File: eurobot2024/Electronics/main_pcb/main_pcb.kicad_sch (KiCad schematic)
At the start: 58 parts, among them J1 PI40HAT, J10 Conn_01x02_Male, J11 Conn_01x03_Male, J12 Conn_01x02_Male, J13 Conn_01x02_Male, J15 Conn_01x02_Male, J16 Conn_01x02_Male, J17 Conn_01x03_Male, J18 Conn_01x03_Male, J2 Conn_01x02_Male, J2 Conn_01x04_Male, J20 Conn_01x05, J21 Conn_01x05, J22 Conn_01x05, J23 22-03-5035, J24 Conn_01x02_Male, J3 Conn_01x02_Male, J4 Conn_01x02_Male, J5 Conn_01x02_Male, J6 Conn_01x02_Male, J8 Conn_01x02_Male, J9 22-03-5035, P1 R-78Bxx-2.0, P2 Amazon 10A stepdown, Q1 NVTR4503NT1G, Q2 NVTR4503NT1G, Q3 NVTR4503NT1G, Q7 NVTR4503NT1G, U1 SN74LVC1G125DBVR, U2 SN74LVC1G04DBVR, U3 PCA9306D, U4 Pololu_MAX14870, U5 PCA9685PW, U6 Pololu_MAX14870, U7 SN74AHCT1G126DBVR

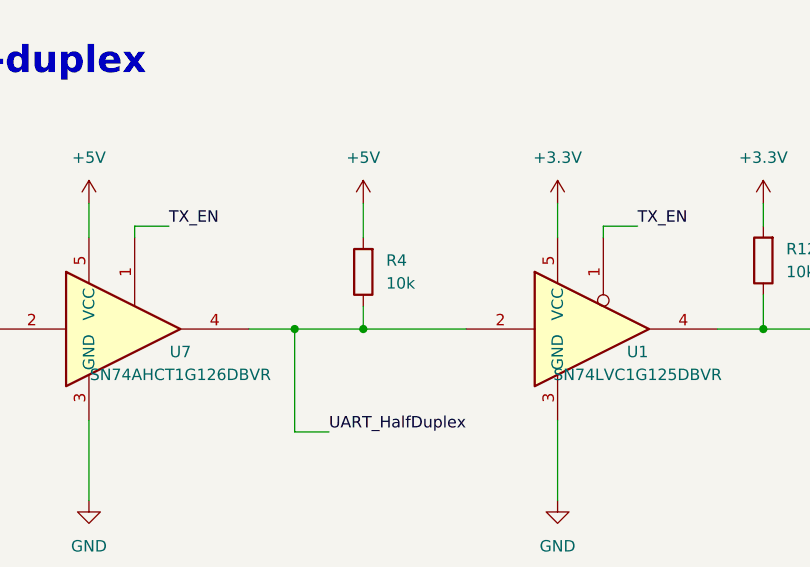
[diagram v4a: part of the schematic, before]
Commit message: STS servo: increase pullup to correct communication ; cleanup code.
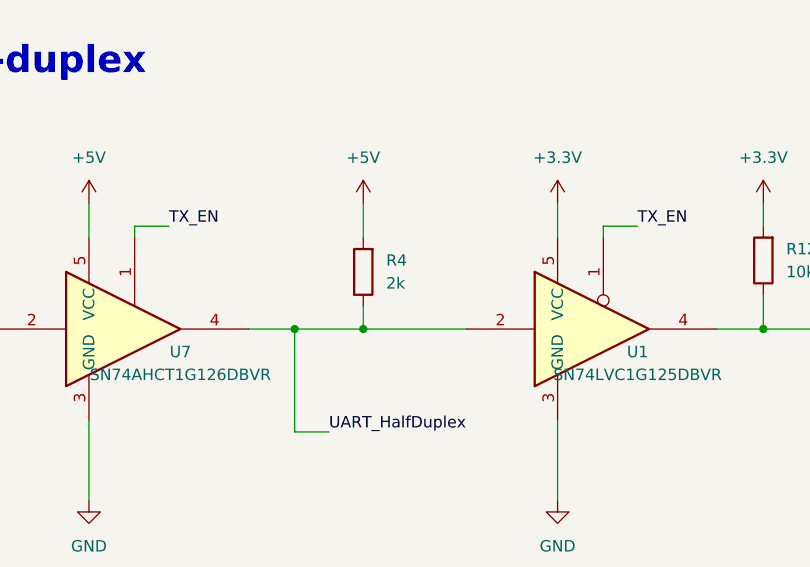
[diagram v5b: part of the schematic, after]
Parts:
- R4: value 10k -> 2k
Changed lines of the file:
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@@
       (effects (font (size 1.27 1.27)) (justify right))
     )
-    (property "Value" "10k" (at 228.6 43.1799 0)
+    (property "Value" "2k" (at 228.6 43.1799 0)
       (effects (font (size 1.27 1.27)) (justify right))
     )

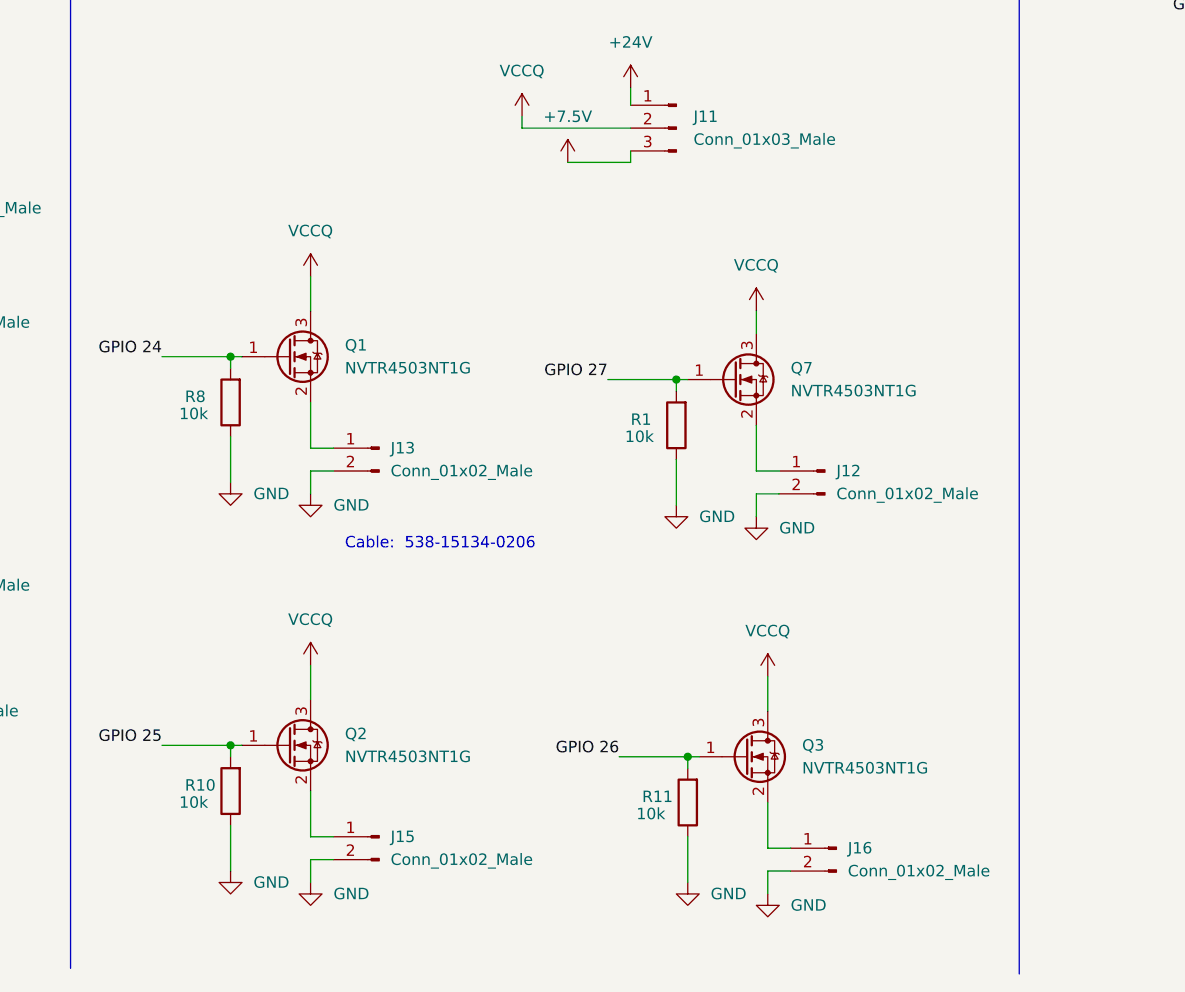
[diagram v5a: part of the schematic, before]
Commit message: [Electronics] Fix main PCB ; add power mosfet PCB
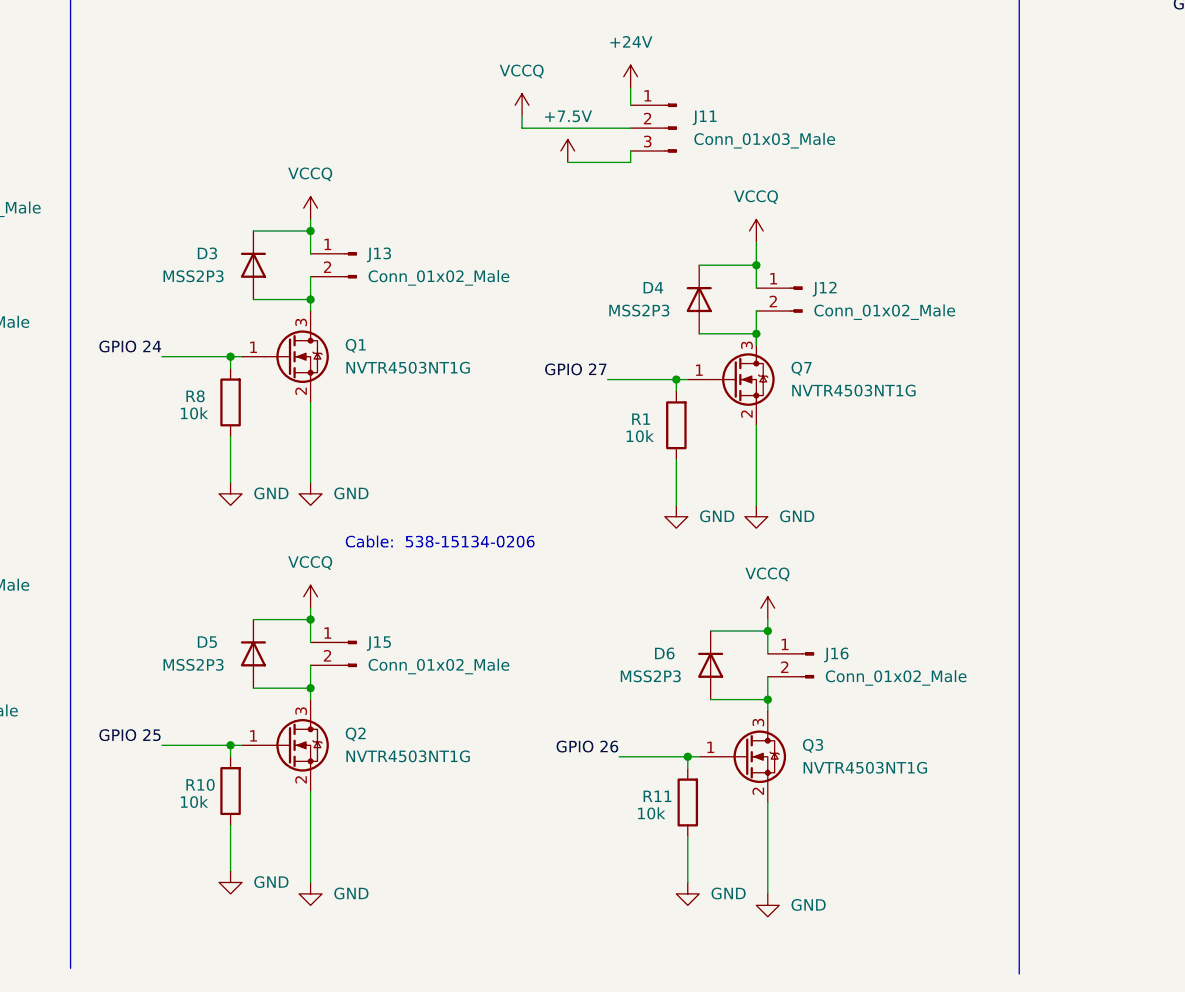
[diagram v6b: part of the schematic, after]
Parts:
- added D3, D4, D5, D6: MSS2P3, Diode_SMD:D_MicroSMP_AK, symbol Device:D
- J15, J16: Mouser Part Number (none) -> 538-53047-0210
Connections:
- net GND: now also Q1.2 (S), Q2.2 (S), Q3.2 (S), Q7.2 (S); no longer J12.2 (Pin_2), J13.2 (Pin_2), J15.2 (Pin_2), J16.2 (Pin_2)
- net VCCQ: now also J12.1 (Pin_1), J13.1 (Pin_1), J15.1 (Pin_1), J16.1 (Pin_1), D3.1 (K), D4.1 (K), D5.1 (K), D6.1 (K); no longer Q1.3 (D), Q2.3 (D), Q3.3 (D), Q7.3 (D)
- new net: D4.2 (A), J12.2 (Pin_2), Q7.3 (D)
- new net: D5.2 (A), J15.2 (Pin_2), Q2.3 (D)
- new net: D6.2 (A), J16.2 (Pin_2), Q3.3 (D)
- new net: D3.2 (A), J13.2 (Pin_2), Q1.3 (D)
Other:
- moved on the sheet: J13
